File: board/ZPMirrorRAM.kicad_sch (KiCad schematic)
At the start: 15 parts, among them IC1 74LS219, IC2 74LS219, IC3 74LS219, IC4 74LS219, U13 74F08, U24 74F20, U26 74LS154, U27 74F138

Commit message: Board V1.1G
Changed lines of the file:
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@@
 (kicad_sch
-	(version 20231120)
+	(version 20250114)
 	(generator "eeschema")
-	(generator_version "8.0")
+	(generator_version "9.0")
 	(paper "USLetter")
 	(title_block
 		(title "ZeroPage $00/$01 Mirror Memory and RAM/ROM Bank Logic")
 		(date "2025-03-04")
-		(rev "1.0F")
+		(rev "1.1A")
 		(company "Data Tuning")
 		(comment 1 "Hydra 16")

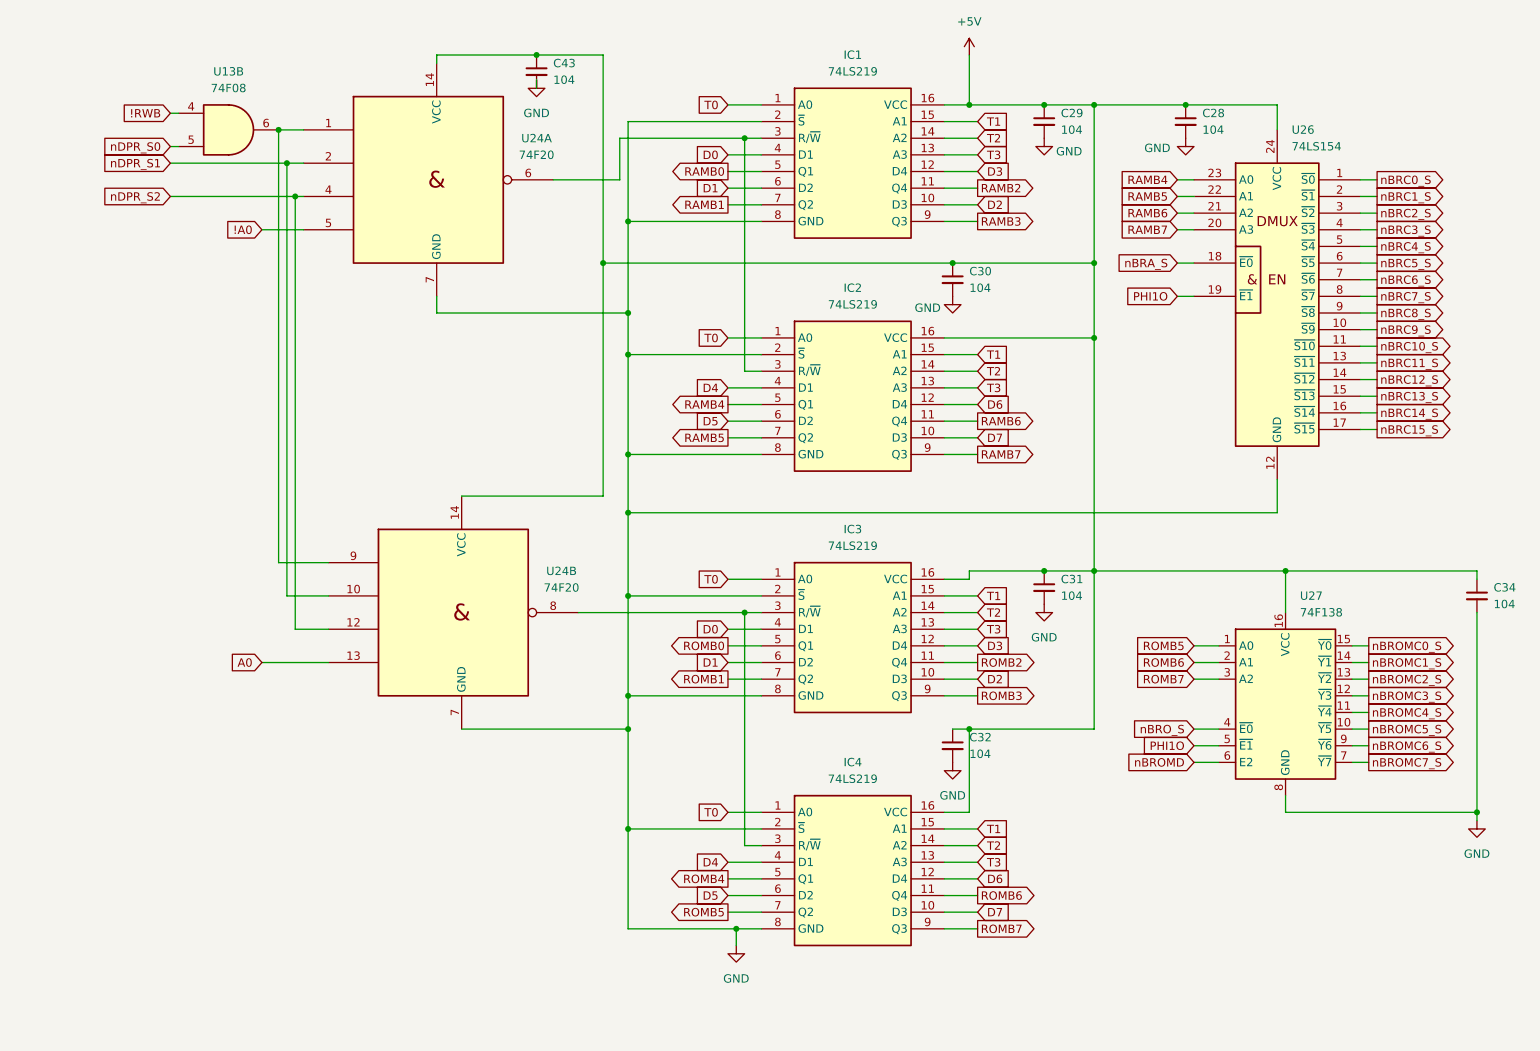
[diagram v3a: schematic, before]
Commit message: V1.3C without board traces
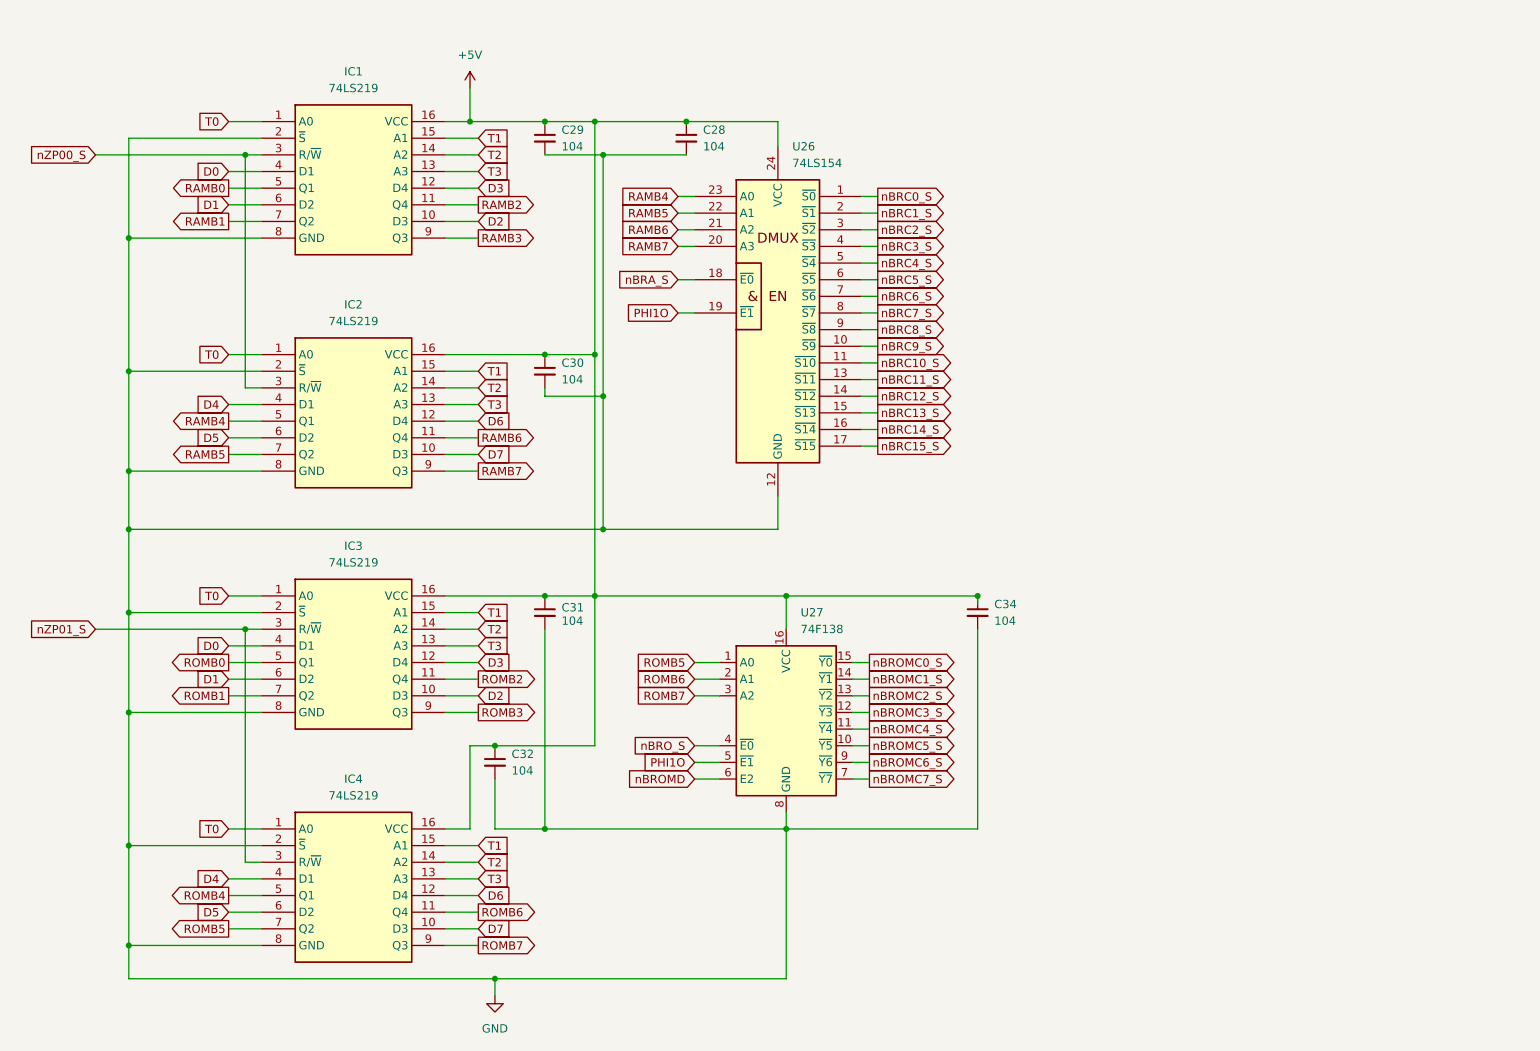
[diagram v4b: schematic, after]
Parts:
- removed C43: 104, Capacitor_THT:C_Disc_D5.0mm_W2.5mm_P5.00mm, symbol Device:C_Small
- removed U13: 74F08, Package_DIP:DIP-14_W7.62mm_Socket_LongPads, symbol 74xx:74LS08
- removed U24: 74F20, Package_DIP:DIP-14_W7.62mm_Socket_LongPads, symbol 74xx_IEEE:7420
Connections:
- net nZP00_S: now reaches IC1.3 (R/~{W}), IC2.3 (R/~{W})
- net nZP01_S: now reaches IC3.3 (R/~{W}), IC4.3 (R/~{W})
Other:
- moved on the sheet: C28, C29, C30, C31, C32, C34, IC1, IC2, IC3, IC4, U26, U27

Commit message: Version 1.7A: More rearrangement, partial wiring of PDB, addition of W register
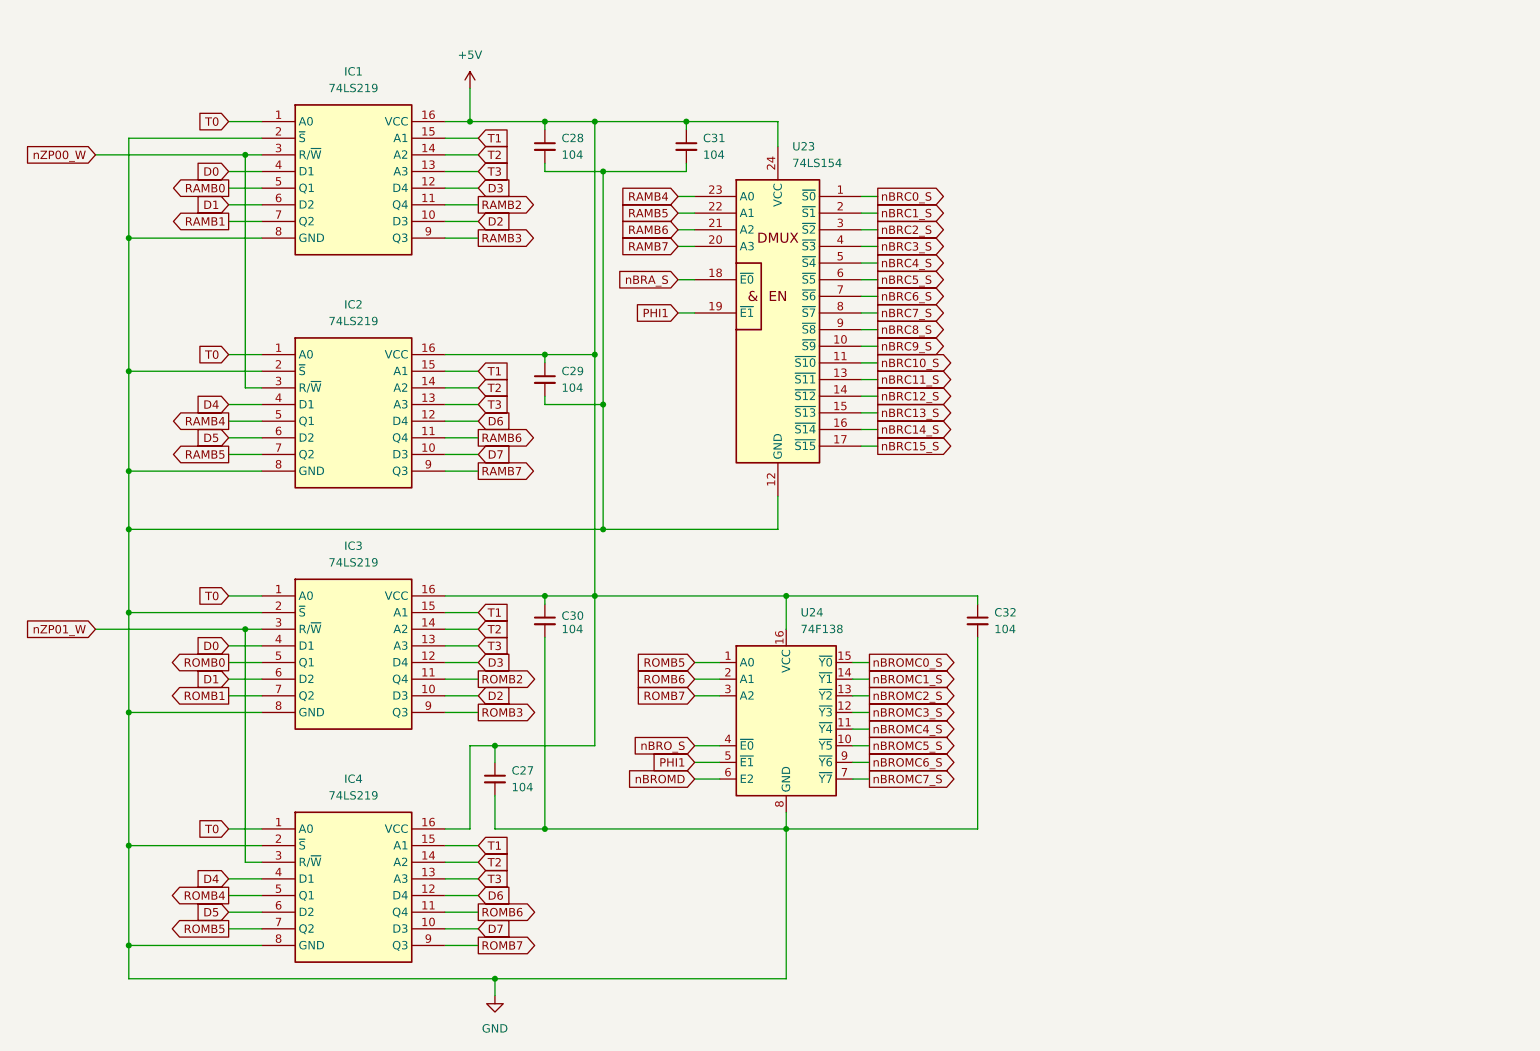
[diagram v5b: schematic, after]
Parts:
- renumbered C32 to C27, C29 to C28, C30 to C29, C31 to C30, C28 to C31, C34 to C32, U26 to U23, U27 to U24
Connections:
- net PHI1O renamed PHI1
- net nZP00_S renamed nZP00_W
- net nZP01_S renamed nZP01_W
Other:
- moved on the sheet: C27, C28, C29, C30, C31, C32

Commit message: Version 1.7A: Partial wireup
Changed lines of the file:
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@@
 		(title "ZeroPage $00/$01 Mirror Memory and RAM/ROM Bank Logic")
 		(date "2025-09-18")
-		(rev "1.6F")
+		(rev "1.7A")
 		(company "Data Tuning")
 		(comment 1 "Hydra 16")
@@
 		)
 		(stroke
+			(width 0)
+			(type default)
+		)
+	)
+	(wire
+		(pts
+			(xy 255.27 151.13) (xy 254 151.13)
+		)
+		(stroke

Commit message: 1.7C: Logic corrections and placement tweaks
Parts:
- added U16: 74F32, Package_DIP:DIP-14_W7.62mm_Socket_LongPads, symbol 74xx:74LS32
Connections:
- net nZP00_W: no longer names the net of IC1.3 (R/~{W}), IC2.3 (R/~{W})
- net nZP00_W: now also U16.6
- net nZP01_W: no longer names the net of IC3.3 (R/~{W}), IC4.3 (R/~{W})
- net nZP01_W: now also U16.11
- new net !A0: U16.13
- new net A0: U16.5
- new net nZPR_W: U16.12, U16.4
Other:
- moved on the sheet: C27, C28, C29, C30, C31, C32, IC1, IC2, IC3, IC4, U23, U24
